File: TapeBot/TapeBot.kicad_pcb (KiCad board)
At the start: 4 copper layers, 99.6 x 101.6 mm, 70 parts, among them IC1 L7805ABD2T-TR, J1 43045-0412, J10 CON_9652068_MOL, J11 CON_9652068_MOL, J12 CON_9652068_MOL, J2 43045-0412, J3 Barrel_Jack, J4 Conn_01x02, J5 Conn_01x02, J6 CON_9652068_MOL, J7 CON_9652068_MOL, J8 CON_9652068_MOL, J9 CON_9652068_MOL, Q1 MMBT4403, Q2 MMBT4403, U1 HX711HX711, U2 HX711HX711, U3 Teensy4.1, U4 TB6612FNG, U5 TB6612FNG, U6 TB6612FNG, U7 TB6612FNG

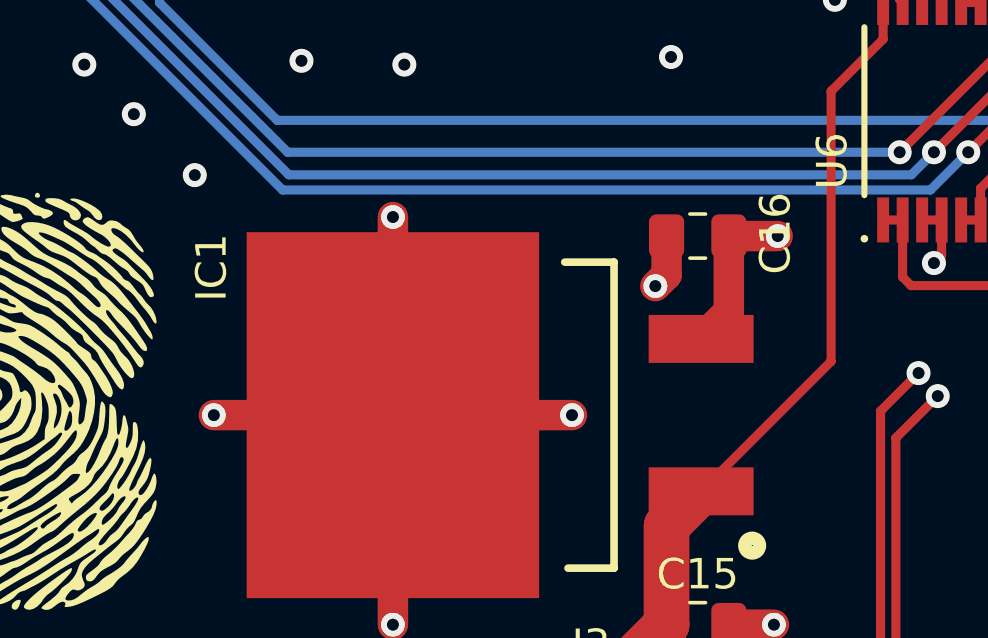
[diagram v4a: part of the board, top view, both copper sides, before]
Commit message: Fixed some footprints
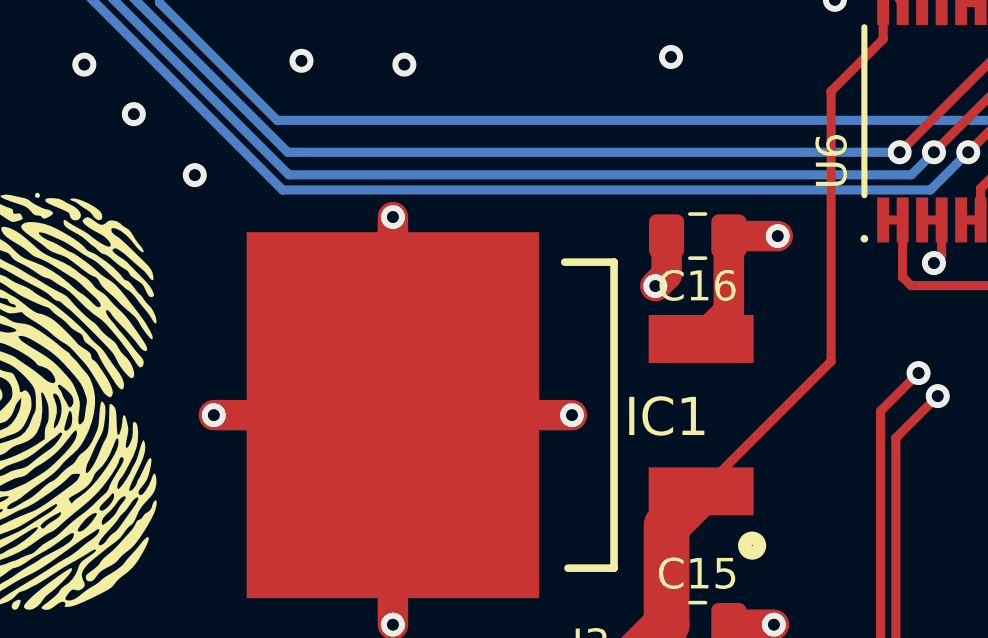
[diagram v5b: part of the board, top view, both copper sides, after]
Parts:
- J10, J11, J12, J6, J7, J8, J9: value CON_9652068_MOL -> 9652068
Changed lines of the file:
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@@
     (property "Sheetname" "Teensy")
     (attr smd)
-    (fp_text reference "C16" (at -2.5902 0.0912 90) (layer "F.SilkS")
-      (effects (font (size 1.016 1.016) (thickness 0.1524)))
+    (fp_text reference "C16" (at 0 -1.68 180) (layer "F.SilkS")
+      (effects (font (size 1 1) (thickness 0.15)))
     )
-    (fp_text value "0.1µF" (at 0 1.68) (layer "F.Fab")
+    (fp_text value "0.1µF" (at 0 1.68 180) (layer "F.Fab")
       (effects (font (size 1 1) (thickness 0.15)))
     )
-    (fp_text user "${REFERENCE}" (at 0 0) (layer "F.Fab")
+    (fp_text user "${REFERENCE}" (at 0 0 180) (layer "F.Fab")
       (effects (font (size 0.5 0.5) (thickness 0.08)))
     )
-    (fp_line (start -0.261252 0.735) (end 0.261252 0.735) (layer "F.SilkS") (width 0.12))
     (fp_line (start -0.261252 -0.735) (end 0.261252 -0.735) (layer "F.SilkS") (width 0.12))
-    (fp_line (start -1.88 -0.98) (end 1.88 -0.98) (layer "F.CrtYd") (width 0.05))
+    (fp_line (start -0.261252 0.735) (end 0.261252 0.735) (layer "F.SilkS") (width 0.12))
     (fp_line (start 1.88 0.98) (end -1.88 0.98) (layer "F.CrtYd") (width 0.05))
-    (fp_line (start -1.88 0.98) (end -1.88 -0.98) (layer "F.CrtYd") (width 0.05))
+    (fp_line (start -1.88 -0.98) (end 1.88 -0.98) (layer "F.CrtYd") (width 0.05))
     (fp_line (start 1.88 -0.98) (end 1.88 0.98) (layer "F.CrtYd") (width 0.05))
+    (fp_line (start -1.88 0.98) (end -1.88 -0.98) (layer "F.CrtYd") (width 0.05))
     (fp_line (start 1 0.625) (end -1 0.625) (layer "F.Fab") (width 0.1))
     (fp_line (start -1 0.625) (end -1 -0.625) (layer "F.Fab") (width 0.1))
-    (fp_line (start 1 -0.625) (end 1 0.625) (layer "F.Fab") (width 0.1))
     (fp_line (start -1 -0.625) (end 1 -0.625) (layer "F.Fab") (width 0.1))
+    (fp_line (start 1 -0.625) (end 1 0.625) (layer "F.Fab") (width 0.1))
     (pad "1" smd roundrect (at -1.0375 0 180) (size 1.175 1.45) (layers "F.Cu" "F.Paste" "F.Mask") (roundrect_rratio 0.212766)
       (net 97 "+5V") (pintype "passive"))
@@
       (effects (font (size 1.016 1.016) (thickness 0.1524)))
     )
-    (fp_text value "CON_9652068_MOL" (at -9.9 -11.43 90) (layer "F.SilkS") hide
+    (fp_text value "9652068" (at -9.9 -11.43 90) (layer "F.SilkS") hide
       (effects (font (size 1 1) (thickness 0.15)))
     )
@@
       (effects (font (size 1.016 1.016) (thickness 0.1524)))
     )
-    (fp_text value "CON_9652068_MOL" (at -9.9 -11.43 90) (layer "F.SilkS") hide
+    (fp_text value "9652068" (at -9.9 -11.43 90) (layer "F.SilkS") hide
       (effects (font (size 1 1) (thickness 0.15)))
     )
@@
       (effects (font (size 1.016 1.016) (thickness 0.1524)))
     )
-    (fp_text value "CON_9652068_MOL" (at -2.2292 3.2766 90) (layer "F.SilkS") hide
+    (fp_text value "9652068" (at -2.2292 3.2766 90) (layer "F.SilkS") hide
       (effects (font (size 1 1) (thickness 0.15)))
     )
@@
       (effects (font (size 1.016 1.016) (thickness 0.1524)))
     )
-    (fp_text value "CON_9652068_MOL" (at 40.639014 -1.553502 90) (layer "F.SilkS") hide
+    (fp_text value "9652068" (at 40.639014 -1.553502 90) (layer "F.SilkS") hide
       (effects (font (size 1 1) (thickness 0.15)))
     )
@@
       (effects (font (size 1.016 1.016) (thickness 0.1524)))
     )
-    (fp_text value "CON_9652068_MOL" (at -9.9 -11.43) (layer "F.SilkS") hide
+    (fp_text value "9652068" (at -9.9 -11.43) (layer "F.SilkS") hide
       (effects (font (size 1 1) (thickness 0.15)))
     )
@@
       (effects (font (size 1.016 1.016) (thickness 0.1524)))
     )
-    (fp_text value "CON_9652068_MOL" (at 15.8048 4.0016 90) (layer "F.SilkS") hide
+    (fp_text value "9652068" (at 15.8048 4.0016 90) (layer "F.SilkS") hide
       (effects (font (size 1 1) (thickness 0.15)))
     )
@@
       (effects (font (size 1.016 1.016) (thickness 0.1524)))
     )
-    (fp_text value "CON_9652068_MOL" (at -9.9 -11.43 90) (layer "F.SilkS") hide
+    (fp_text value "9652068" (at -9.9 -11.43 90) (layer "F.SilkS") hide
       (effects (font (size 1 1) (thickness 0.15)))
     )
@@
     (property "Sheetname" "Teensy")
     (attr smd)
-    (fp_text reference "IC1" (at -13.4168 0.1828 90) (layer "F.SilkS")
-      (effects (font (size 1.016 1.016) (thickness 0.1524)))
+    (fp_text reference "IC1" (at 1.753 5.174) (layer "F.SilkS")
+      (effects (font (size 1.27 1.27) (thickness 0.254)))
     )
     (fp_text value "L7805ABD2T-TR" (at 1.753 5.174) (layer "F.SilkS") hide
@@
       (effects (font (size 1.27 1.27) (thickness 0.254)))
     )
-    (fp_line (start 0 10.2) (end -1.535 10.2) (layer "F.SilkS") (width 0.254))
     (fp_line (start 0 0) (end 0 10.2) (layer "F.SilkS") (width 0.254))
     (fp_line (start 0 0) (end -1.644 0) (layer "F.SilkS") (width 0.254))
+    (fp_line (start 0 10.2) (end -1.535 10.2) (layer "F.SilkS") (width 0.254))
     (fp_circle (center 4.603 9.449) (end 4.603 9.668) (layer "F.SilkS") (width 0.5) (fill none))
     (fp_line (start -9.15 10.2) (end -9.15 0) (layer "F.Fab") (width 0.254))
+    (fp_line (start 0 10.2) (end -9.15 10.2) (layer "F.Fab") (width 0.254))
     (fp_line (start -9.15 0) (end 0 0) (layer "F.Fab") (width 0.254))
     (fp_line (start 0 0) (end 0 10.2) (layer "F.Fab") (width 0.254))
-    (fp_line (start 0 10.2) (end -9.15 10.2) (layer "F.Fab") (width 0.254))
     (pad "1" smd rect (at 2.904 7.64 90) (size 1.6 3.5) (layers "F.Cu" "F.Paste" "F.Mask")
       (net 9 "+12V") (pinfunction "INPUT") (pintype "passive"))

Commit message: Final Commit
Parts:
- C1: footprint Capacitor_SMD:C_0603_1608Metric -> Capacitor_SMD:C_0603_1608Metric_Pad1.08x0.95mm_HandSolder
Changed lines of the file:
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@@
     )
   )
-  (footprint "Capacitor_SMD:C_0603_1608Metric" (layer "F.Cu")
+  (footprint "Capacitor_SMD:C_0603_1608Metric_Pad1.08x0.95mm_HandSolder" (layer "F.Cu")
     (at 224.62 104.847)
-    (descr "Capacitor SMD 0603 (1608 Metric), square (rectangular) end terminal, IPC_7351 nominal, (Body size source: IPC-SM-782 page 76, https://www.pcb-3d.com/wordpress/wp-content/uploads/ipc-sm-782a_amendment_1_and_2.pdf), generated with kicad-footprint-generator")
-    (tags "capacitor")
+    (descr "Capacitor SMD 0603 (1608 Metric), square (rectangular) end terminal, IPC_7351 nominal with elongated pad for handsoldering. (Body size source: IPC-SM-782 page 76, https://www.pcb-3d.com/wordpress/wp-content/uploads/ipc-sm-782a_amendment_1_and_2.pdf), generated with kicad-footprint-generator")
+    (tags "capacitor handsolder")
     (property "Sheetfile" "LoadCells.kicad_sch")
     (property "Sheetname" "LoadCells")
     (attr smd)
-    (fp_text reference "C1" (at -2.624 -0.072) (layer "F.SilkS")
-      (effects (font (size 1.016 1.016) (thickness 0.1524)))
-    )
-    (fp_text value "0.1uF" (at 0 1.43) (layer "F.Fab") hide
+    (fp_text reference "C1" (at 0 -1.43) (layer "F.SilkS")
+      (effects (font (size 1 1) (thickness 0.15)))
+    )
+    (fp_text value "0.1uF" (at 0 1.43) (layer "F.Fab")
       (effects (font (size 1 1) (thickness 0.15)))
     )
@@
       (effects (font (size 0.4 0.4) (thickness 0.06)))
     )
-    (fp_line (start -0.14058 -0.51) (end 0.14058 -0.51) (layer "F.SilkS") (width 0.12))
-    (fp_line (start -0.14058 0.51) (end 0.14058 0.51) (layer "F.SilkS") (width 0.12))
-    (fp_line (start 1.48 0.73) (end -1.48 0.73) (layer "F.CrtYd") (width 0.05))
-    (fp_line (start 1.48 -0.73) (end 1.48 0.73) (layer "F.CrtYd") (width 0.05))
-    (fp_line (start -1.48 0.73) (end -1.48 -0.73) (layer "F.CrtYd") (width 0.05))
-    (fp_line (start -1.48 -0.73) (end 1.48 -0.73) (layer "F.CrtYd") (width 0.05))
-    (fp_line (start -0.8 -0.4) (end 0.8 -0.4) (layer "F.Fab") (width 0.1))
-    (fp_line (start 0.8 -0.4) (end 0.8 0.4) (layer "F.Fab") (width 0.1))
-    (fp_line (start -0.8 0.4) (end -0.8 -0.4) (layer "F.Fab") (width 0.1))
-    (fp_line (start 0.8 0.4) (end -0.8 0.4) (layer "F.Fab") (width 0.1))
-    (pad "1" smd roundrect (at -0.775 0) (size 0.9 0.95) (layers "F.Cu" "F.Paste" "F.Mask") (roundrect_rratio 0.25)
+    (fp_line (start -0.146267 -0.51) (end 0.146267 -0.51) (layer "F.SilkS") (width 0.12))
+    (fp_line (start -0.146267 0.51) (end 0.146267 0.51) (layer "F.SilkS") (width 0.12))
+    (fp_line (start 1.65 0.73) (end -1.65 0.73) (layer "F.CrtYd") (width 0.05))
+    (fp_line (start 1.65 -0.73) (end 1.65 0.73) (layer "F.CrtYd") (width 0.05))
+    (fp_line (start -1.65 -0.73) (end 1.65 -0.73) (layer "F.CrtYd") (width 0.05))
+    (fp_line (start -1.65 0.73) (end -1.65 -0.73) (layer "F.CrtYd") (width 0.05))
+    (fp_line (start -0.8 0.4) (end -0.8 -0.4) (layer "F.Fab") (width 0.1))
+    (fp_line (start -0.8 -0.4) (end 0.8 -0.4) (layer "F.Fab") (width 0.1))
+    (fp_line (start 0.8 0.4) (end -0.8 0.4) (layer "F.Fab") (width 0.1))
+    (fp_line (start 0.8 -0.4) (end 0.8 0.4) (layer "F.Fab") (width 0.1))
+    (pad "1" smd roundrect (at -0.8625 0) (size 1.075 0.95) (layers "F.Cu" "F.Paste" "F.Mask") (roundrect_rratio 0.25)
       (net 1 "/LoadCells/AVDD1") (pinfunction "1") (pintype "passive"))
-    (pad "2" smd roundrect (at 0.775 0) (size 0.9 0.95) (layers "F.Cu" "F.Paste" "F.Mask") (roundrect_rratio 0.25)
+    (pad "2" smd roundrect (at 0.8625 0) (size 1.075 0.95) (layers "F.Cu" "F.Paste" "F.Mask") (roundrect_rratio 0.25)
       (net 2 "GND") (pinfunction "2") (pintype "passive"))
     (model "${KICAD6_3DMODEL_DIR}/Capacitor_SMD.3dshapes/C_0603_1608Metric.wrl"
@@
       (effects (font (size 1.27 1.27) (thickness 0.254)))
     )
-    (fp_line (start 0 0) (end 0 10.2) (layer "F.SilkS") (width 0.254))
     (fp_line (start 0 0) (end -1.644 0) (layer "F.SilkS") (width 0.254))
     (fp_line (start 0 10.2) (end -1.535 10.2) (layer "F.SilkS") (width 0.254))
+    (fp_line (start 0 0) (end 0 10.2) (layer "F.SilkS") (width 0.254))
     (fp_circle (center 4.603 9.449) (end 4.603 9.668) (layer "F.SilkS") (width 0.5) (fill none))
+    (fp_line (start 0 10.2) (end -9.15 10.2) (layer "F.Fab") (width 0.254))
+    (fp_line (start 0 0) (end 0 10.2) (layer "F.Fab") (width 0.254))
     (fp_line (start -9.15 10.2) (end -9.15 0) (layer "F.Fab") (width 0.254))
-    (fp_line (start 0 10.2) (end -9.15 10.2) (layer "F.Fab") (width 0.254))
     (fp_line (start -9.15 0) (end 0 0) (layer "F.Fab") (width 0.254))
-    (fp_line (start 0 0) (end 0 10.2) (layer "F.Fab") (width 0.254))
     (pad "1" smd rect (at 2.904 7.64 90) (size 1.6 3.5) (layers "F.Cu" "F.Paste" "F.Mask")
       (net 9 "+12V") (pinfunction "INPUT") (pintype "passive"))
